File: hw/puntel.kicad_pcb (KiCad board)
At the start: 2 copper layers, 101.6 x 20.3 mm, 48 parts, among them J2 STRIP-3, J3 USB-power, J4 USB-prog, J5 STRIP-4, J6 STRIP-4, Q1 DTA114, SW1 BUTTON, SW2 BUTTON, U1 AP2111H, U10 LM75BD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

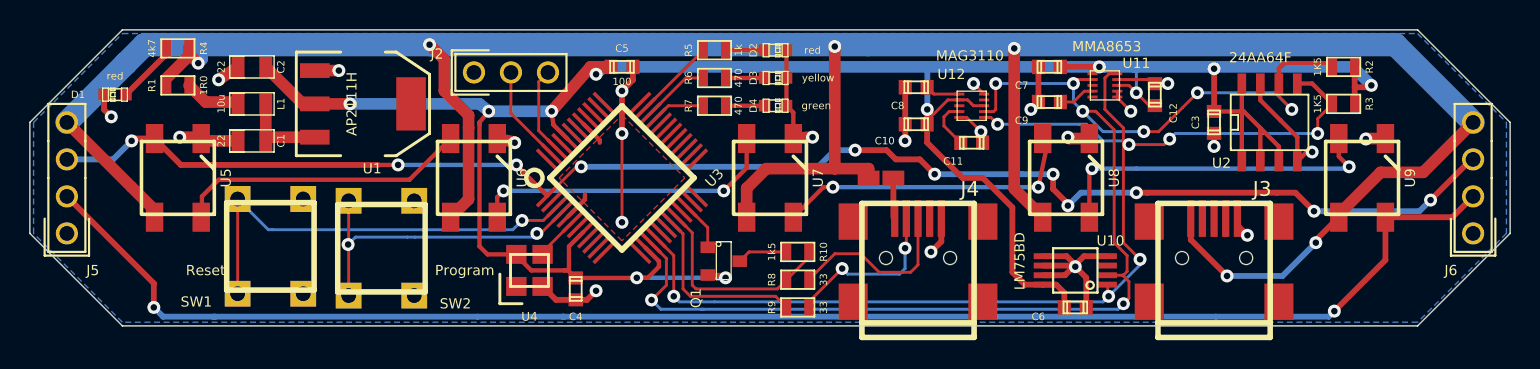
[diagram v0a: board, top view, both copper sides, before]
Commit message: hw: clean-up pcb
Signed-off-by: Alessandro Rubini <rubini@gnudd.com>
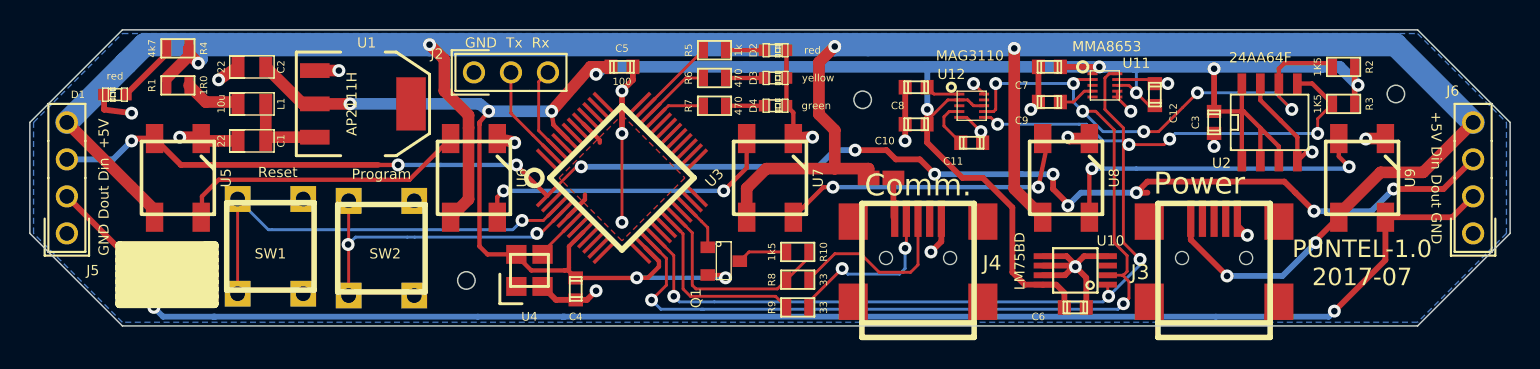
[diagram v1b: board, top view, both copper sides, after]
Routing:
- net +3.3V: track 178.6 -> 176.8 mm
- net /Din: track 104.8 -> 106.2 mm
- net GND: track 81.7 -> 82.9 mm
- net +5V: track 188.4 -> 189.3 mm
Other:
- outline, holes or cut-outs redrawn
- board text added: "+5V Din Dout GND"
- board text added: "Comm."
- board text added: "GND Dout Din +5V"
- board text added: "GND Tx Rx"
- board text added: "PUNTEL-1.0 2017-07"
- board text added: "Power"
